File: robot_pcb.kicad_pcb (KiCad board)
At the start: 2 copper layers, 145 parts, among them J1 Raspberry_Pi_2_3, J10 Servo_TrayRelease, J11 BATT BYPASS, J12 12V BYPASS, J13 MAX14870, J14 MAX14870, J15 MAX14870, J16 MAX14870, J17 Conn_01x04, J18 USB_C_Receptacle_PowerOnly_6P, J19 3V3 BYPASS, J2 Motor FL, J20 5V BYPASS, J21 5.1V BYPASS, J24 Motor FR, J25 ConductClaw, J27 TOF_Front, J28 OLED_Display, J3 Lipo, J4 Motor BL, J5 Motor BR, J6 TOF_Claw, J7 UltraS_Side, J8 Servo_Grab, J9 Servo_Lift, Q2 Q_NMOS_GDS, SW1 SW_SPDT, SW2 SW_Push, U1 STM32F407VGTx, U10 DMG2305UX-7, U11 DMG2305UX-7, U2 BQ76920PW, U3 AP64501SP-13, U4 MAX25240AFFD/VY+, U5 DMG2305UX-7, U6 AP64501SP-13, U7 AP64501SP-13, U9 BNO086, Y1 25MHz, Y2 32.768kHz

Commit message: flipped battery connectors
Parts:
- BT1, J3: moved to B.Cu
- moved BT1 0.29 mm to (73.4, 199.9)

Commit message: changes
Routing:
- net /Battery/TS1_SW: track 2.25 -> 8.05 mm
- net +BATT: track 61.3 -> 63.9 mm
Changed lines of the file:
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@@
+	)
+	(segment
+		(start 80.95 193.9)
+		(end 80.95 193.899)
+		(width 0.5)
+		(layer "F.Cu")
+		(net 1)
 	)
 	(segment
@@
 		(start 81.415 200.165)
 		(end 73.575 200.165)
+		(width 0.5)
+		(layer "F.Cu")
+		(net 1)
+	)
+	(segment
+		(start 82.8 195.75)
+		(end 80.95 193.9)
 		(width 0.5)
 		(layer "F.Cu")
@@
 	(segment
 		(start 94.2865 193.899)
+		(end 80.95 193.899)
+		(width 0.5)
+		(layer "F.Cu")
+		(net 1)
+	)
+	(segment
+		(start 80.95 193.899)
 		(end 79.841 193.899)
 		(width 0.5)
@@
 	)
 	(segment
+		(start 86.8 201.55)
+		(end 86.8 195.75)
+		(width 0.5)
+		(layer "F.Cu")
+		(net 113)
+	)
+	(segment
 		(start 103.290001 193.995)
 		(end 101.4635 195.821501)
@@
 	)
 	(segment
+		(start 97.29 203.8)
+		(end 96.795 203.8)
+		(width 0.5)
+		(layer "F.Cu")
+		(net 228)
+	)
+	(segment
 		(start 92.155 207.45)
 		(end 92.65 207.945)
@@
 	)
 	(segment
-		(start 97.29 203.8)
-		(end 96.795 203.8)
-		(width 0.3)
-		(layer "F.Cu")
-		(net 228)
-	)
-	(segment
 		(start 96.795 203.8)
 		(end 92.65 207.945)
-		(width 0.3)
+		(width 0.5)
 		(layer "F.Cu")
 		(net 228)
 	)
 	(segment
-		(start 99.39 203.785)
-		(end 103.55 207.945)
-		(width 0.2)
-		(layer "F.Cu")
-		(net 229)
-	)
-	(segment
 		(start 99.25 203.785)
-		(end 98.325 203.785)
-		(width 0.2)
+		(end 99.39 203.785)
+		(width 0.5)
 		(layer "F.Cu")
 		(net 229)
@@
 		(start 99.235 203.8)
 		(end 99.25 203.785)
-		(width 0.2)
+		(width 0.5)
+		(layer "F.Cu")
+		(net 229)
+	)
+	(segment
+		(start 98.31 203.8)
+		(end 99.235 203.8)
+		(width 0.5)
 		(layer "F.Cu")
 		(net 229)
@@
 	)
 	(segment
-		(start 99.25 203.785)
-		(end 99.39 203.785)
-		(width 0.2)
+		(start 99.39 203.785)
+		(end 103.55 207.945)
+		(width 0.5)
 		(layer "F.Cu")
 		(net 229)

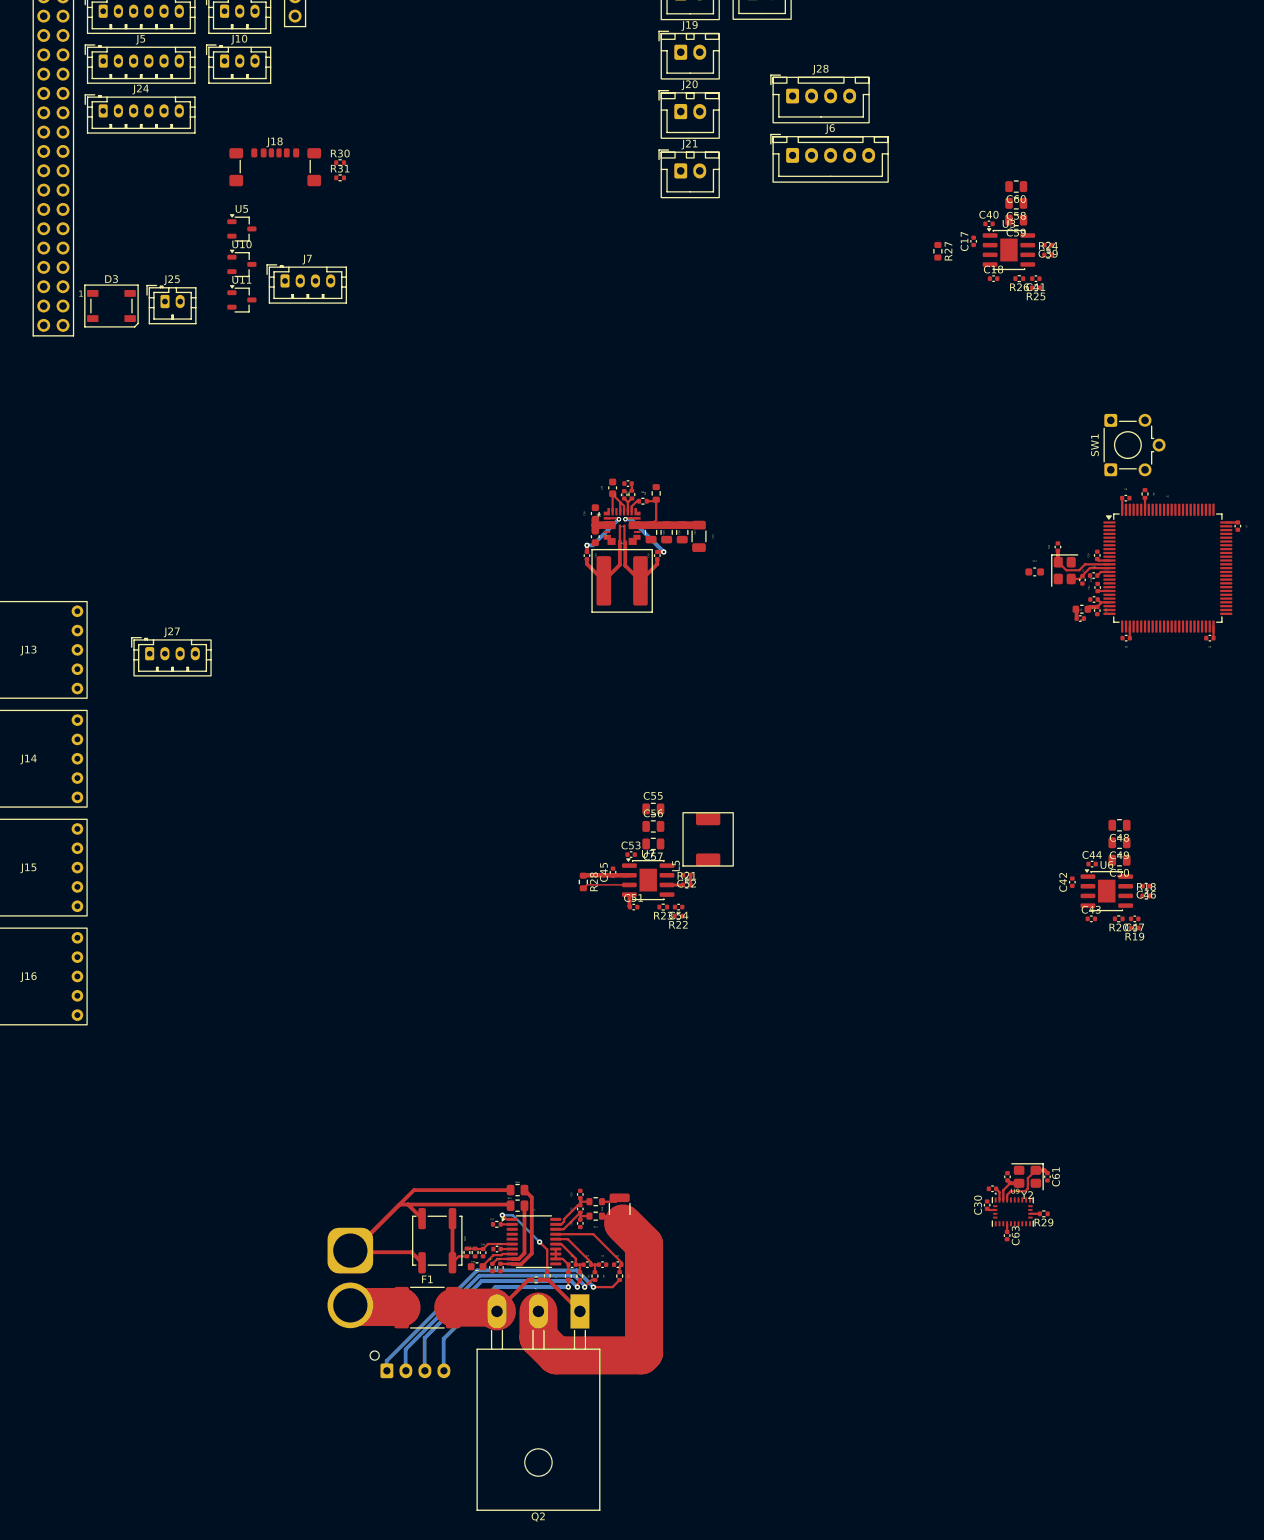
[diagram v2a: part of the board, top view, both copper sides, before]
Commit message: added board outline
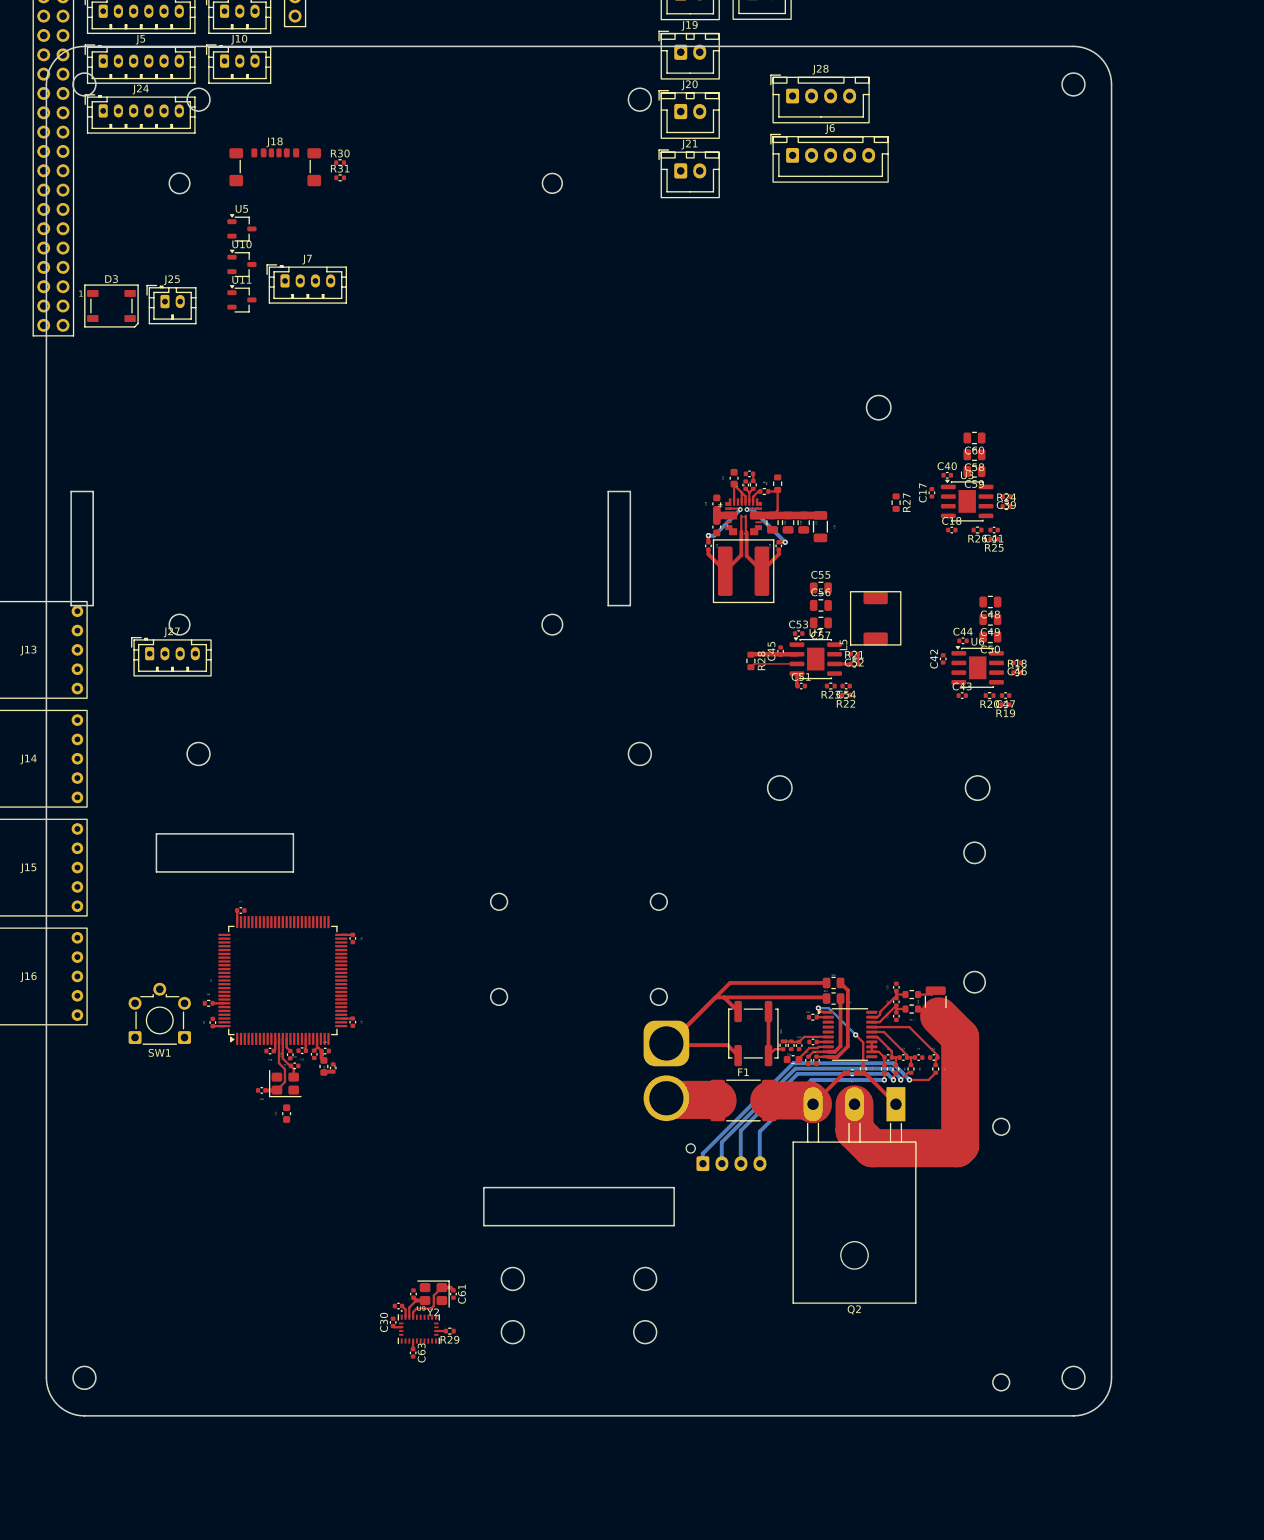
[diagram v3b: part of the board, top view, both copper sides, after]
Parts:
- moved SW1 142.8 mm to (51.6, 171.9), turned to 180 degrees
- moved C7 140.5 mm to (59.0, 155.2), turned to 0 degrees
- moved R6 140.1 mm to (54.8, 167.4), turned to 0 degrees
- moved C8 138.4 mm to (55.3, 170.0), turned to 90 degrees
- moved U1 128.3 mm to (64.5, 164.4), turned to 90 degrees
- moved C10 126.8 mm to (62.8, 173.7), turned to 180 degrees
- moved C69 126.7 mm to (61.7, 178.9), turned to 180 degrees
- moved C16 123.0 mm to (65.5, 174.2), turned to 90 degrees
- moved Y1 122.6 mm to (64.8, 178.0), turned to 0 degrees
- moved C70 121.7 mm to (66.0, 175.7), turned to 0 degrees
- moved C12 121.4 mm to (65.0, 181.9), turned to 90 degrees
- moved C11 121.0 mm to (67.0, 173.7), turned to 180 degrees
- moved C6 119.4 mm to (73.7, 158.9), turned to -90 degrees
- moved C13 118.7 mm to (68.6, 174.2), turned to -90 degrees
- moved C14 116.8 mm to (70.1, 173.7), turned to 0 degrees
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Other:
- board outline added: 140 x 180 mm

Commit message: moved some stuff to roughly where it will be
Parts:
- J13, J14, J15, J16, J2, J24, J4, J5: moved to B.Cu
- moved J2 206.8 mm to (126.7, 218.7), turned to 90 degrees
- moved J17 176.1 mm to (73.3, 206.0)
- moved J24 167.1 mm to (66.6, 215.2), turned to 90 degrees
- moved J13 141.9 mm to (138.1, 214.2), turned to 180 degrees
- moved J15 128.0 mm to (113.5, 51.6), turned to 180 degrees
- moved J16 122.9 mm to (82.7, 52.4), turned to 180 degrees
- moved J7 121.4 mm to (168.8, 135.2), turned to 90 degrees
- moved J27 109.0 mm to (121.0, 201.5)
- moved J1 81.6 mm to (99.8, 77.1)
- moved J14 78.2 mm to (54.0, 210.1), turned to 180 degrees
- moved R5 77.4 mm to (141.4, 99.2), turned to 0 degrees
- moved Q2 76.3 mm to (146.1, 104.4), turned to -90 degrees
- moved C1 75.8 mm to (139.9, 99.5), turned to 90 degrees
- moved R4 73.8 mm to (141.4, 102.5), turned to 0 degrees
- moved C4 73.6 mm to (139.9, 101.5), turned to 90 degrees
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
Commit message: idrk what i changed tbh but probably not anything important
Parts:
- moved J9 132.9 mm to (148.7, 180.7), turned to 90 degrees
- moved J8 130.8 mm to (148.7, 171.1), turned to 90 degrees
- moved J10 123.8 mm to (142.2, 180.8), turned to 90 degrees
- moved J24 17.3 mm to (58.9, 199.8), turned to 180 degrees
- moved J2 15.4 mm to (130.8, 203.8), turned to 180 degrees
- moved J13 12.1 mm to (126.0, 214.2)
- moved J27 4.99 mm to (120.4, 196.6)

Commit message: add new board dxf
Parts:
- J3: footprint Connector_JST:JST_XH_B4B-XH-AM_1x04_P2.50mm_Vertical -> Connector_JST:JST_XH_B4B-XH-A_1x04_P2.50mm_Vertical
- J6: footprint Connector_JST:JST_XH_B5B-XH-A_1x05_P2.50mm_Vertical -> Connector_JST:JST_PH_B5B-PH-K_1x05_P2.00mm_Vertical
- J7: moved to B.Cu
- moved J25 161.7 mm to (168.2, 184.6)
- moved D2 156.0 mm to (171.2, 154.0), turned to 90 degrees
- moved D3 153.6 mm to (169.8, 160.9), turned to 90 degrees
- moved C47 135.4 mm to (268.6, 194.7)
- moved C48 135.4 mm to (266.6, 182.4)
- moved C49 135.4 mm to (266.6, 184.7)
- moved C50 135.4 mm to (266.6, 187.0)
- moved R19 135.4 mm to (268.6, 195.9)
- moved C44 135.4 mm to (263.0, 187.5)
- moved C46 135.4 mm to (270.1, 190.4)
- moved R18 135.4 mm to (270.1, 191.7)
- moved R20 135.4 mm to (266.5, 194.7)
- moved U6 135.4 mm to (264.9, 191.1)
- moved C42 135.4 mm to (260.4, 189.9)
- moved C43 135.4 mm to (262.9, 194.7)
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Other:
- board outline removed

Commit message: update pcb and schematic
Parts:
- added J22: Down_LEDs, Connector_JST:JST_PH_B2B-PH-K_1x02_P2.00mm_Vertical, B.Cu at (105.0, 145.0)
- moved U5 89.2 mm to (98.0, 146.0), turned to 180 degrees
- moved J17 41.1 mm to (37.0, 186.8), turned to 180 degrees
- moved J15 36.0 mm to (124.0, 86.0)
- moved J4 33.8 mm to (138.0, 45.5)
- moved J28 33.1 mm to (158.5, 29.0)
- moved J16 23.9 mm to (75.0, 75.0)
- moved J10 19.7 mm to (167.0, 58.0), turned to 90 degrees
- moved J5 18.8 mm to (70.0, 45.5)
- moved SW1 6.25 mm to (36.6, 198.2)

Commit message: oled
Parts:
- J28: footprint Connector_JST:JST_XH_B4B-XH-A_1x04_P2.50mm_Vertical -> Dry_Lettuce:OLED_small
- moved J28 194.4 mm to (58.0, 195.4)
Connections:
- net Net-(D1-DIN) renamed /GPIO10
- U5 pad 2: unconnected-(U5-S-Pad2) -> +5V
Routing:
- net /Battery/DSG_DRAIN: track 39.1 -> 35.9 mm
